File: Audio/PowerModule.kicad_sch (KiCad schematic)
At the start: 15 parts, among them J4 PWR_IN, J5 PWR_OUT, U1 TEC 3-1223

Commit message: PowerModuleのU1プロパティ入れ子崩れを直し、回路図が開けるようにする。
TEC 3-1223 載せ替え時に U1 の Description プロパティの effects が閉じられず、
Manufacturer と MPN がその内側に入り込んでいた。括弧の総数は合っていたため
気付きにくいが、KiCad は Description の effects 内に property を許さずエラーになる。

Co-authored-by: m_arino <indare@users.noreply.github.com>
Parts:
- U1: MPN (none) -> TEC 3-1223; Manufacturer (none) -> Traco Power
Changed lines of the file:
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@@
 					(size 1.27 1.27)
 				)
+			)
+		)
 		(property "Manufacturer" "Traco Power"
 			(at 64.77 31.75 0)
@@
 			)
 		)
-			)
-		)

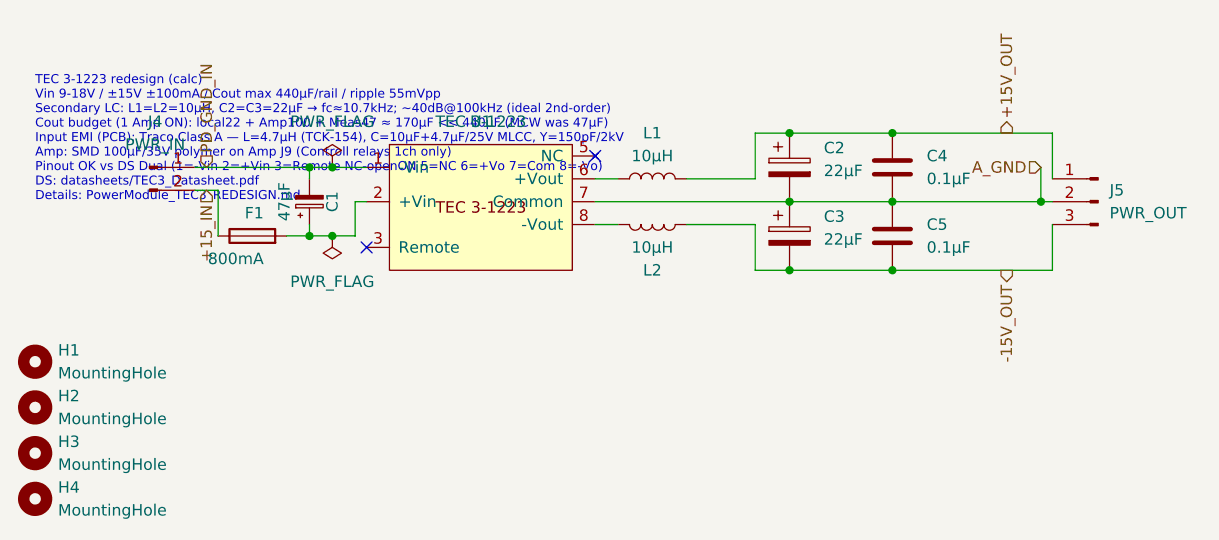
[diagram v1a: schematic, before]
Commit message: PowerModuleのL1/L2を秋月114977（DFE322512F-100M）に指定する。
二次LC用10µHをムラタ DFE322512F（3.2×2.5、シールド、1.1A、DCR 324mΩ）に固定し、
推奨ランドの専用FPへ差し替える。

Co-authored-by: m_arino <indare@users.noreply.github.com>
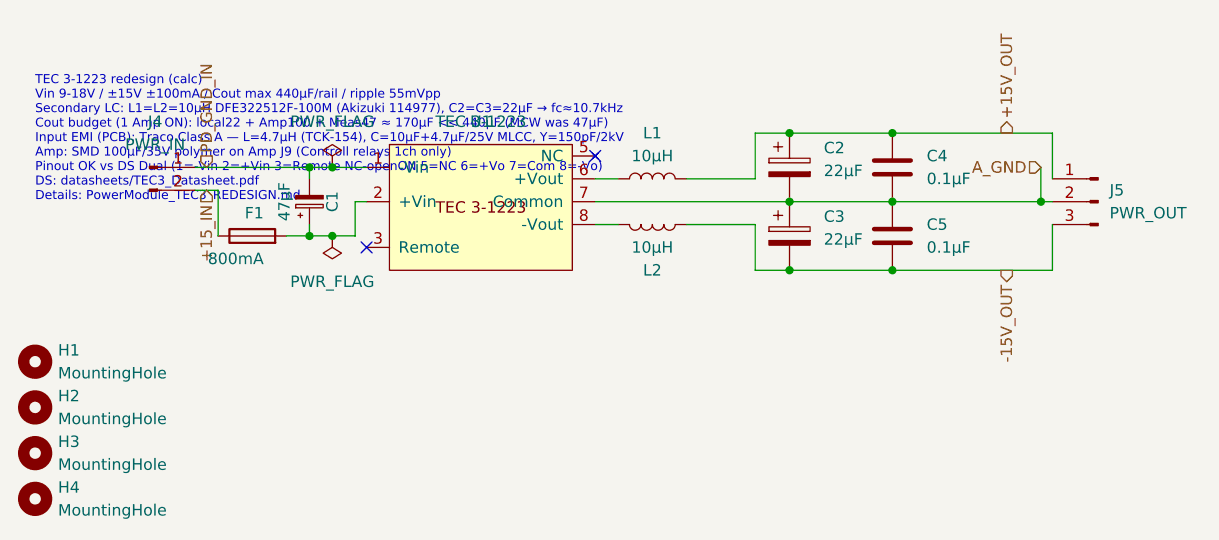
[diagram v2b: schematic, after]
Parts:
- L1, L2: footprint Inductor_SMD:L_1210_3225Metric -> Library:L_Murata_DFE322512F; MPN (none) -> DFE322512F-100M; Manufacturer (none) -> Murata
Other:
- note added: "TEC 3-1223 redesign (calc) Vin 9-18V / ±15V ±100mA / Cout max 440µF/rail / ripple 55mVpp Secondary LC: L1=L2=10µH DFE322512F-100M (Akizuki 114977), C2=C3=22µF → fc≈10.7kHz Cout budget (1 Amp ON): local22 + Amp100 + Meas47 ≈ 170µF << 440µF (MCW was 47µF) Input EMI (PCB): Traco Class A — L=4.7µH (TCK-154), C=10µF+4.7µF/25V MLCC, Y=150pF/2kV Amp: SMD 100µF/35V polymer on Amp J9 (Controll relays 1ch 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"
- note removed: "TEC 3-1223 redesign (calc) Vin 9-18V / ±15V ±100mA / Cout max 440µF/rail / ripple 55mVpp Secondary LC: L1=L2=10µH, C2=C3=22µF → fc≈10.7kHz; ~40dB@100kHz (ideal 2nd-order) Cout budget (1 Amp ON): local22 + Amp100 + Meas47 ≈ 170µF << 440µF (MCW was 47µF) Input EMI (PCB): Traco Class A — L=4.7µH (TCK-154), C=10µF+4.7µF/25V MLCC, Y=150pF/2kV Amp: SMD 100µF/35V polymer on Amp J9 (Controll relays 1ch o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"
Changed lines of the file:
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@@
 		)
 	)
-	(text "TEC 3-1223 redesign (calc)\nVin 9-18V / ±15V ±100mA / Cout max 440µF/rail / ripple 55mVpp\nSecondary LC: L1=L2=10µH, C2=C3=22µF → fc≈10.7kHz; ~40dB@100kHz (ideal 2nd-order)\nCout budget (1 Amp ON): local22 + Amp100 + Meas47 ≈ 170µF << 440µF (MCW was 47µF)\nInput EMI (PCB): Traco Class A — L=4.7µH (TCK-154), C=10µF+4.7µF/25V MLCC, Y=150pF/2kV\nAmp: SMD 100µF/35V polymer on Amp J9 (Controll relays 1ch only)\nPinout OK vs DS Dual (1=-Vin 2=+Vin 3=Remote NC-openON 5=NC 6=+Vo 7=Com 8=-Vo)\nDS: datasheets/TEC3_Datasheet.pdf\nDetails: PowerModule_TEC3_REDESIGN.md"
+	(text "TEC 3-1223 redesign (calc)\nVin 9-18V / ±15V ±100mA / Cout max 440µF/rail / ripple 55mVpp\nSecondary LC: L1=L2=10µH DFE322512F-100M (Akizuki 114977), C2=C3=22µF → fc≈10.7kHz\nCout budget (1 Amp ON): local22 + Amp100 + Meas47 ≈ 170µF << 440µF (MCW was 47µF)\nInput EMI (PCB): Traco Class A — L=4.7µH (TCK-154), C=10µF+4.7µF/25V MLCC, Y=150pF/2kV\nAmp: SMD 100µF/35V polymer on Amp J9 (Controll relays 1ch only)\nPinout OK vs DS Dual (1=-Vin 2=+Vin 3=Remote NC-openON 5=NC 6=+Vo 7=Com 8=-Vo)\nDS: datasheets/TEC3_Datasheet.pdf\nDetails: PowerModule_TEC3_REDESIGN.md"
 		(exclude_from_sim no)
 		(at 15.24 26.67 0)
@@
 			)
 		)
-		(property "Footprint" "Inductor_SMD:L_1210_3225Metric"
+		(property "Footprint" "Library:L_Murata_DFE322512F"
 			(at 83.82 38.1 0)
 			(hide yes)
@@
 			)
 		)
-		(property "Datasheet" ""
+		(property "Datasheet" "https://akizukidenshi.com/catalog/g/g114977/"
 			(at 83.82 38.1 0)
 			(hide yes)
@@
 			)
 		)
-		(property "Description" "Secondary LC +15: shielded 10uH, Isat>=0.3A. fc~10.7kHz with C2=22uF"
+		(property "Description" "Akizuki 114977 Murata DFE322512F-100M 10uH 1.1A DCR 324mOhm metal shielded. Secondary LC +15, fc~10.7kHz with C2=22uF"
+			(at 83.82 38.1 0)
+			(hide yes)
+			(show_name no)
+			(do_not_autoplace no)
+			(effects
+				(font
+					(size 1.27 1.27)
+				)
+			)
+		)
+		(property "Manufacturer" "Murata"
+			(at 83.82 38.1 0)
+			(hide yes)
+			(show_name no)
+			(do_not_autoplace no)
+			(effects
+				(font
+					(size 1.27 1.27)
+				)
+			)
+		)
+		(property "MPN" "DFE322512F-100M"
 			(at 83.82 38.1 0)
 			(hide yes)
@@
 			)
 		)
-		(property "Footprint" "Inductor_SMD:L_1210_3225Metric"
+		(property "Footprint" "Library:L_Murata_DFE322512F"
 			(at 83.82 43.18 0)
 			(hide yes)
@@
 			)
 		)
-		(property "Datasheet" ""
+		(property "Datasheet" "https://akizukidenshi.com/catalog/g/g114977/"
 			(at 83.82 43.18 0)
 			(hide yes)
@@
 			)
 		)
-		(property "Description" "Secondary LC -15: shielded 10uH, Isat>=0.3A. fc~10.7kHz with C3=22uF"
+		(property "Description" "Akizuki 114977 Murata DFE322512F-100M 10uH 1.1A DCR 324mOhm metal shielded. Secondary LC -15, fc~10.7kHz with C3=22uF"
 			(at 83.82 43.18 0)
 			(hide yes)
+			(show_name no)
+			(do_not_autoplace no)
+			(effects
+				(font
+					(size 1.27 1.27)
+				)
+			)
+		)
+		(property "Manufacturer" "Murata"
+			(at 83.82 43.18 0)
+			(hide yes)
+			(show_name no)
+			(do_not_autoplace no)
+			(effects
+				(font
+					(size 1.27 1.27)
+				)
+			)
+		)
+		(property "MPN" "DFE322512F-100M"
+			(at 83.82 43.18 0)
+			(hide yes)
